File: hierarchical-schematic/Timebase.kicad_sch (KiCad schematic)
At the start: 59 parts, among them J402 Jack-DC, J404 Jack-DC, J8 Conn_Coaxial, J9 Conn_Coaxial, U401 LM358, U402 LM358, U403 LM358

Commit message: improvements to hierarchical schematic
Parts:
- removed H1, H2, H3, H4: MountingHole_Pad, MountingHole:MountingHole_2.7mm_M2.5_DIN965_Pad_TopOnly, symbol Mechanical:MountingHole_Pad
- removed J402, J404: Jack-DC, SnapEDA Library:CUI_PJ-007, symbol Connector:Jack-DC
- removed V401: DC 15, SnapEDA Library:CUI_PJ-009A, symbol pspice:VSOURCE
- removed V402: DC -15, SnapEDA Library:CUI_PJ-009A, symbol pspice:VSOURCE
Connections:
- net Out: no longer names the net of J9.1 (In), R416.2
- net V+15 renamed +15
- net V-15 renamed -15
- net VCO_Out: no longer names the net of D408.1 (K), J8.1 (In), R429.2
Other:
- note removed: ".options gmin=1e-10 .options abstol=1e-10 .tran 10m 500m"
- note removed: ".param Rt=10k set=0.9 .param Rt2=10k set2=0.5 .param Rt3=5k set3=0.5 .param Rt4=10k set4=0.9 .param Rt5=5k set5=0.9 .param Rt6=5k set6=0.5"
- note removed: "Mechanicals"
- note removed: "Power"
- note removed: "Settings for Pots"
- note removed: "Simulation Commands"

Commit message: 2ndmixer-2ndlo
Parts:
- renumbered U402 to U403
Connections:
- net +15 renamed +15 Regulated
- net -15 renamed -15 Regulated
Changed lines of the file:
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@@
     (stroke (width 0) (type default) (color 0 0 0 0))
   )
-  (wire (pts (xy 67.31 135.89) (xy 67.31 138.43))
+  (wire (pts (xy 67.31 135.89) (xy 67.31 142.875))
     (stroke (width 0) (type default) (color 0 0 0 0))
   )
@@
     (stroke (width 0) (type default) (color 0 0 0 0))
   )
-  (wire (pts (xy 255.27 62.23) (xy 260.35 62.23))
+  (wire (pts (xy 254.635 62.23) (xy 260.35 62.23))
     (stroke (width 0) (type default) (color 0 0 0 0))
   )
@@
     (effects (font (size 1.27 1.27)) (justify left bottom))
   )
-  (global_label "-15" (shape input) (at 190.5 99.06 0) (fields_autoplaced)
+  (hierarchical_label "-15 Regulated" (shape input) (at 281.94 101.6 0)
     (effects (font (size 1.27 1.27)) (justify left))
-    (property "Intersheet References" "${INTERSHEET_REFS}" (id 0) (at 196.9045 98.9806 0)
-      (effects (font (size 1.27 1.27)) (justify left) hide)
-    )
-  )
-  (global_label "-15" (shape input) (at 281.94 101.6 270) (fields_autoplaced)
+  )
+  (hierarchical_label "-15 Regulated" (shape input) (at 190.5 99.06 0)
+    (effects (font (size 1.27 1.27)) (justify left))
+  )
+  (hierarchical_label "-15 Regulated" (shape input) (at 158.75 173.99 0)
+    (effects (font (size 1.27 1.27)) (justify left))
+  )
+  (hierarchical_label "-15 Regulated" (shape input) (at 67.31 142.875 180)
     (effects (font (size 1.27 1.27)) (justify right))
-    (property "Intersheet References" "${INTERSHEET_REFS}" (id 0) (at 281.8606 108.0045 90)
-      (effects (font (size 1.27 1.27)) (justify right) hide)
-    )
-  )
-  (global_label "-15" (shape input) (at 54.61 181.61 0) (fields_autoplaced)
+  )
+  (hierarchical_label "-15 Regulated" (shape input) (at 54.61 181.61 0)
     (effects (font (size 1.27 1.27)) (justify left))
-    (property "Intersheet References" "${INTERSHEET_REFS}" (id 0) (at 61.0145 181.5306 0)
-      (effects (font (size 1.27 1.27)) (justify left) hide)
-    )
-  )
-  (global_label "+15" (shape input) (at 138.43 99.06 180) (fields_autoplaced)
+  )
+  (hierarchical_label "+15 Regulated" (shape input) (at 138.43 99.06 180)
     (effects (font (size 1.27 1.27)) (justify right))
-    (property "Intersheet References" "${INTERSHEET_REFS}" (id 0) (at 132.0255 98.9806 0)
-      (effects (font (size 1.27 1.27)) (justify right) hide)
-    )
-  )
-  (global_label "+15" (shape input) (at 255.27 62.23 180) (fields_autoplaced)
+  )
+  (hierarchical_label "+15 Regulated" (shape input) (at 254.635 62.23 270)
     (effects (font (size 1.27 1.27)) (justify right))
-    (property "Intersheet References" "${INTERSHEET_REFS}" (id 0) (at 248.8655 62.1506 0)
-      (effects (font (size 1.27 1.27)) (justify right) hide)
-    )
-  )
-  (global_label "-15" (shape input) (at 158.75 173.99 0) (fields_autoplaced)
-    (effects (font (size 1.27 1.27)) (justify left))
-    (property "Intersheet References" "${INTERSHEET_REFS}" (id 0) (at 165.1545 173.9106 0)
-      (effects (font (size 1.27 1.27)) (justify left) hide)
-    )
-  )
-  (global_label "-15" (shape input) (at 331.47 88.9 0) (fields_autoplaced)
-    (effects (font (size 1.27 1.27)) (justify left))
-    (property "Intersheet References" "${INTERSHEET_REFS}" (id 0) (at 337.8745 88.8206 0)
-      (effects (font (size 1.27 1.27)) (justify left) hide)
-    )
-  )
-  (global_label "-15" (shape input) (at 67.31 138.43 270) (fields_autoplaced)
+  )
+  (hierarchical_label "-15 Regulated" (shape input) (at 331.47 88.9 270)
     (effects (font (size 1.27 1.27)) (justify right))
-    (property "Intersheet References" "${INTERSHEET_REFS}" (id 0) (at 67.2306 144.8345 90)
-      (effects (font (size 1.27 1.27)) (justify right) hide)
-    )
   )
   (symbol (lib_id "Connector:Conn_Coaxial") (at 215.9 121.92 0) (unit 1)
@@
   (symbol (lib_id "Amplifier_Operational:LM358") (at 158.75 121.92 0) (unit 2)
     (in_bom yes) (on_board yes)
-    (property "Reference" "U402" (id 0) (at 163.83 118.11 0))
+    (property "Reference" "U403" (id 0) (at 163.83 118.11 0))
     (property "Value" "LM358" (id 1) (at 157.48 121.92 0))
     (property "Footprint" "SnapEDA Library:DIP794W45P254L959H508Q8" (id 2) (at 158.75 121.92 0)

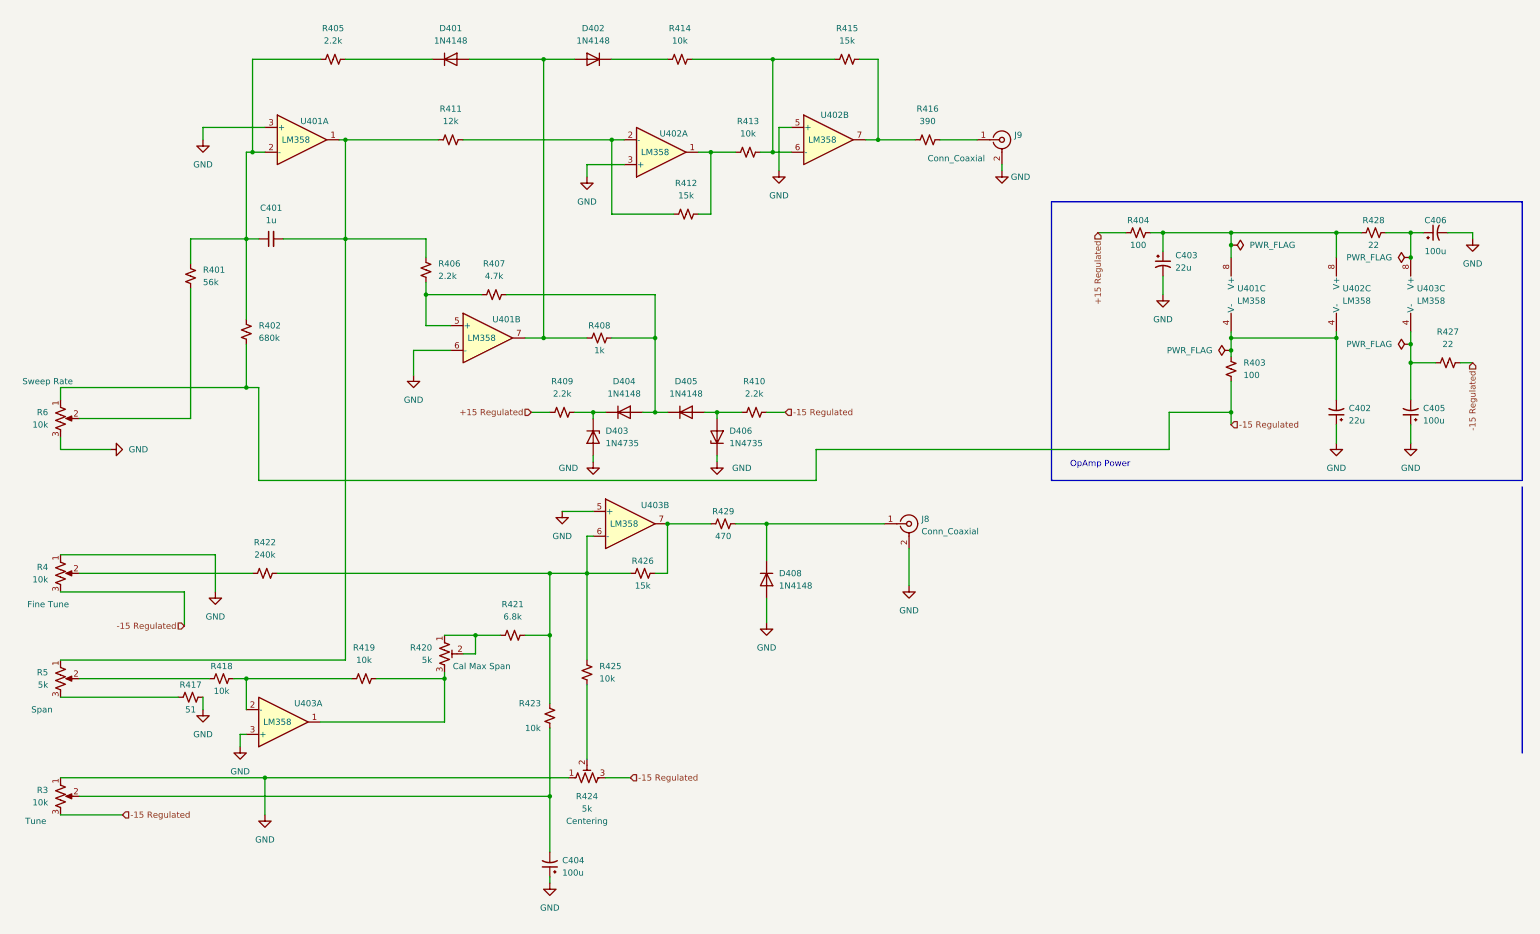
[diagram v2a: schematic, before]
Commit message: improved if and log amp and second lo/mixer
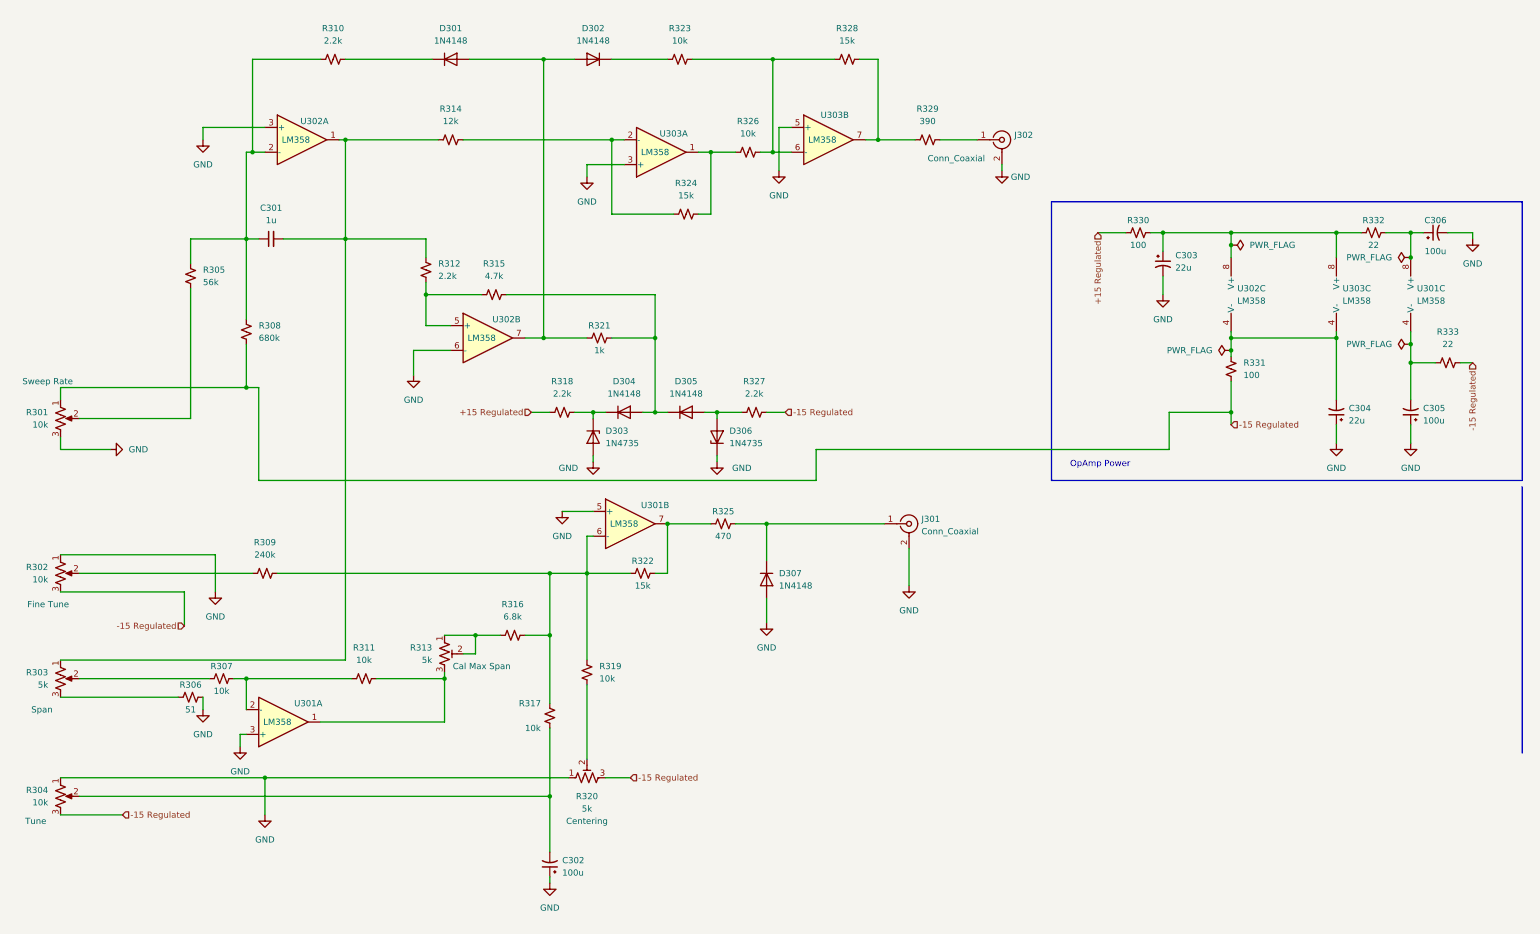
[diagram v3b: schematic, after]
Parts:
- renumbered C401 to C301, C404 to C302, C403 to C303, C402 to C304, C405 to C305, C406 to C306, D401 to D301, D402 to D302, D403 to D303, D404 to D304, D405 to D305, D406 to D306, D408 to D307, J8 to J301, J9 to J302, R6 to R301, R4 to R302, R5 to R303, R3 to R304, R401 to R305, R417 to R306, R418 to R307, R402 to R308, R422 to R309, R405 to R310, R419 to R311, R406 to R312, R420 to R313, R411 to R314, R407 to R315, R421 to R316, R423 to R317, R409 to R318, R425 to R319, R424 to R320, R408 to R321, R426 to R322, R414 to R323, R412 to R324, R429 to R325, R413 to R326, R410 to R327, R415 to R328, R416 to R329, R404 to R330, R403 to R331, R428 to R332, R427 to R333, U403 to U301, U401 to U302, U402 to U303

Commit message: Hierarchical schematic updates
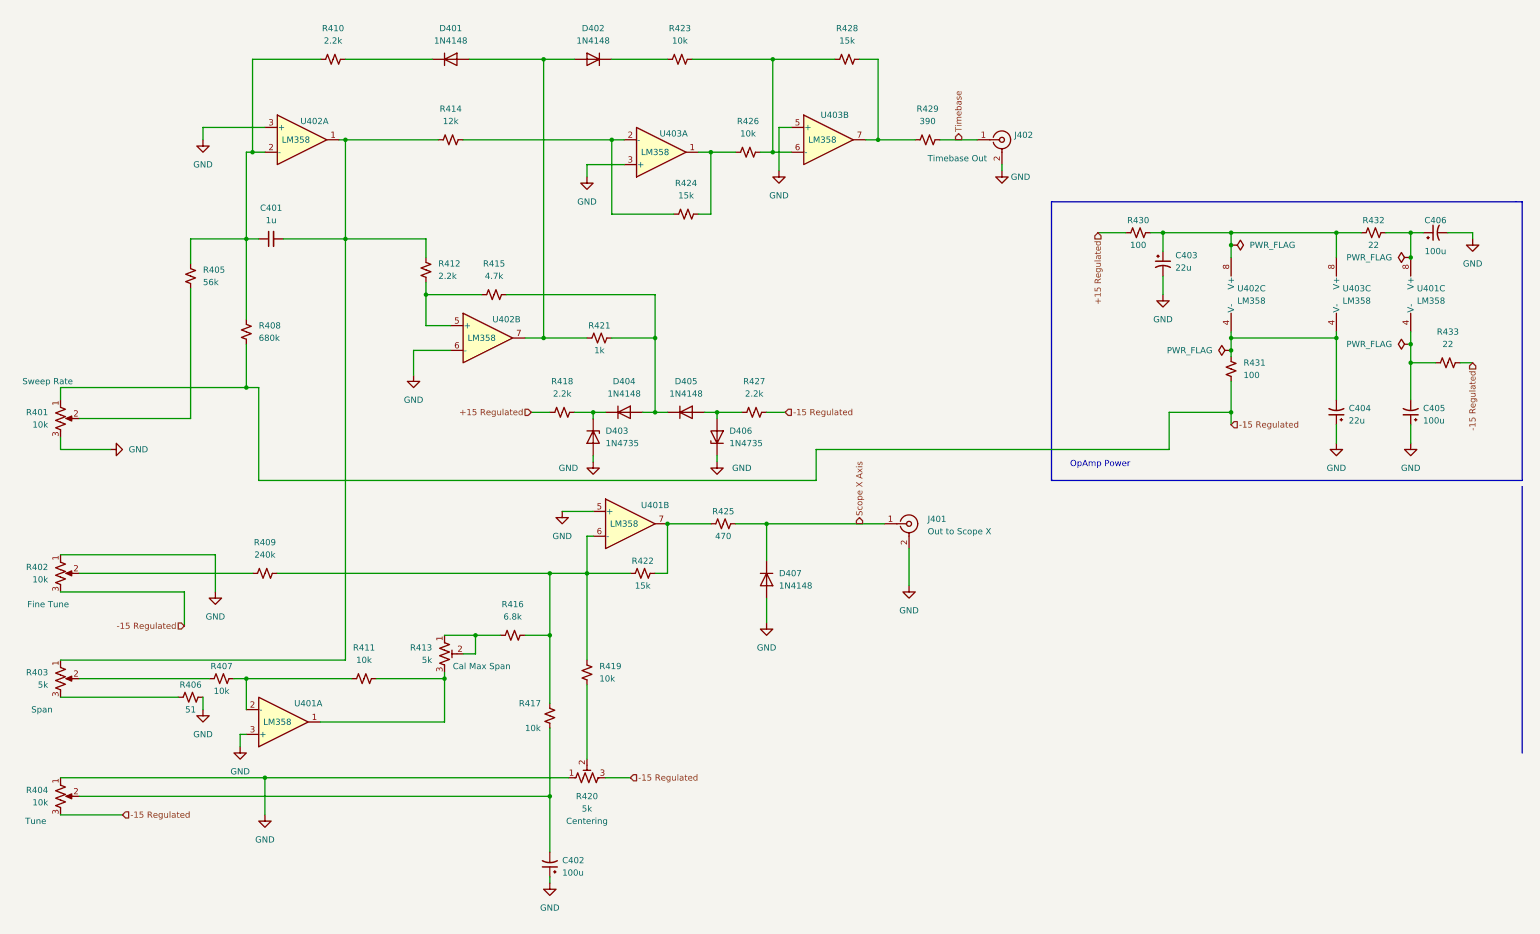
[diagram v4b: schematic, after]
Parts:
- J401: renamed from J301; value Conn_Coaxial -> Out to Scope X
- J402: renamed from J302; value Conn_Coaxial -> Timebase Out
- renumbered C301 to C401, C302 to C402, C303 to C403, C304 to C404, C305 to C405, C306 to C406, D301 to D401, D302 to D402, D303 to D403, D304 to D404, D305 to D405, D306 to D406, D307 to D407, R301 to R401, R302 to R402, R303 to R403, R304 to R404, R305 to R405, R306 to R406, R307 to R407, R308 to R408, R309 to R409, R310 to R410, R311 to R411, R312 to R412, R313 to R413, R314 to R414, R315 to R415, R316 to R416, R317 to R417, R318 to R418, R319 to R419, R320 to R420, R321 to R421, R322 to R422, R323 to R423, R324 to R424, R325 to R425, R326 to R426, R327 to R427, R328 to R428, R329 to R429, R330 to R430, R331 to R431, R332 to R432, R333 to R433, U301 to U401, U302 to U402, U303 to U403
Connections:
- net Scope X Axis: now reaches D407.1 (K), J401.1 (In), R425.2
- net Timebase: now reaches J402.1 (In), R429.2
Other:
- title: Spectrum Analyzer -> Spectrum Analyzer: Timebase

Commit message: appearance improvements
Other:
- moved on the sheet: C401, C402, C406, R404, R406, R407, R408, R409, R415, R420, R424, R428

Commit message: v7 conversion
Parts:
- D401, D402, D404, D405, D407: Spice_Lib_File 1N4148.mod -> (none); Spice_Model D1N4148 -> (none); Spice_Netlist_Enabled Y -> (none); Spice_Node_Sequence 2 1 -> (none); Spice_Primitive D -> (none)
- D403, D406: Spice_Lib_File 1N4735A.lib -> (none); Spice_Model DI_1N4735A -> (none); Spice_Netlist_Enabled Y -> (none); Spice_Node_Sequence 2 1 -> (none); Spice_Primitive X -> (none)
- J401, J402: Spice_Model Conn_Coaxial -> (none); Spice_Netlist_Enabled N -> (none); Spice_Primitive J -> (none)
- R401: Spice_Lib_File Pot.lib -> (none); Spice_Model pot_lin -> (none); Spice_Netlist_Enabled Y -> (none); Spice_Primitive X -> (none)
- R402: Spice_Lib_File Pot2.lib -> (none); Spice_Model pot_lin2 -> (none); Spice_Netlist_Enabled Y -> (none); Spice_Primitive X -> (none)
- R403: Spice_Lib_File Pot3.lib -> (none); Spice_Model pot_lin3 -> (none); Spice_Netlist_Enabled Y -> (none); Spice_Primitive X -> (none)
- R404: Spice_Lib_File Pot4.lib -> (none); Spice_Model pot_lin4 -> (none); Spice_Netlist_Enabled Y -> (none); Spice_Primitive X -> (none)
- R413: Spice_Lib_File Pot6.lib -> (none); Spice_Model pot_lin6 -> (none); Spice_Netlist_Enabled Y -> (none); Spice_Primitive X -> (none)
- R420: Spice_Lib_File Pot5.lib -> (none); Spice_Model pot_lin5 -> (none); Spice_Netlist_Enabled Y -> (none); Spice_Primitive X -> (none)
- U401, U402, U403: Spice_Lib_File TL072-dual.lib -> (none); Spice_Model TL072c -> (none); Spice_Netlist_Enabled Y -> (none); Spice_Primitive X -> (none)
